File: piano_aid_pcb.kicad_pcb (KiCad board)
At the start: 2 copper layers, 101.6 x 63.5 mm, 0 parts

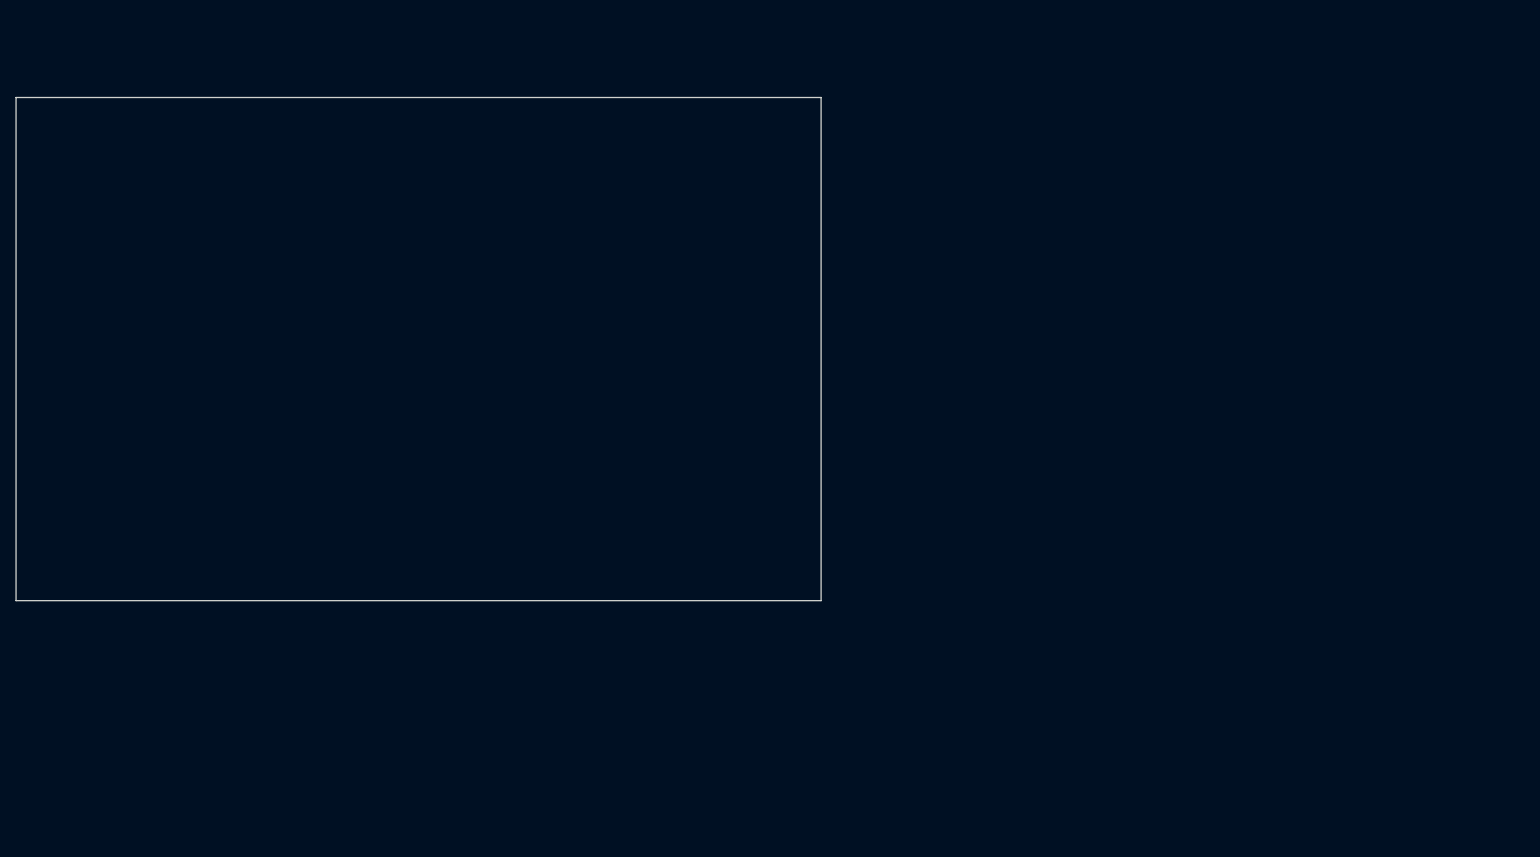
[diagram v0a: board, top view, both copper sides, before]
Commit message: Started board layout. Finished footprints
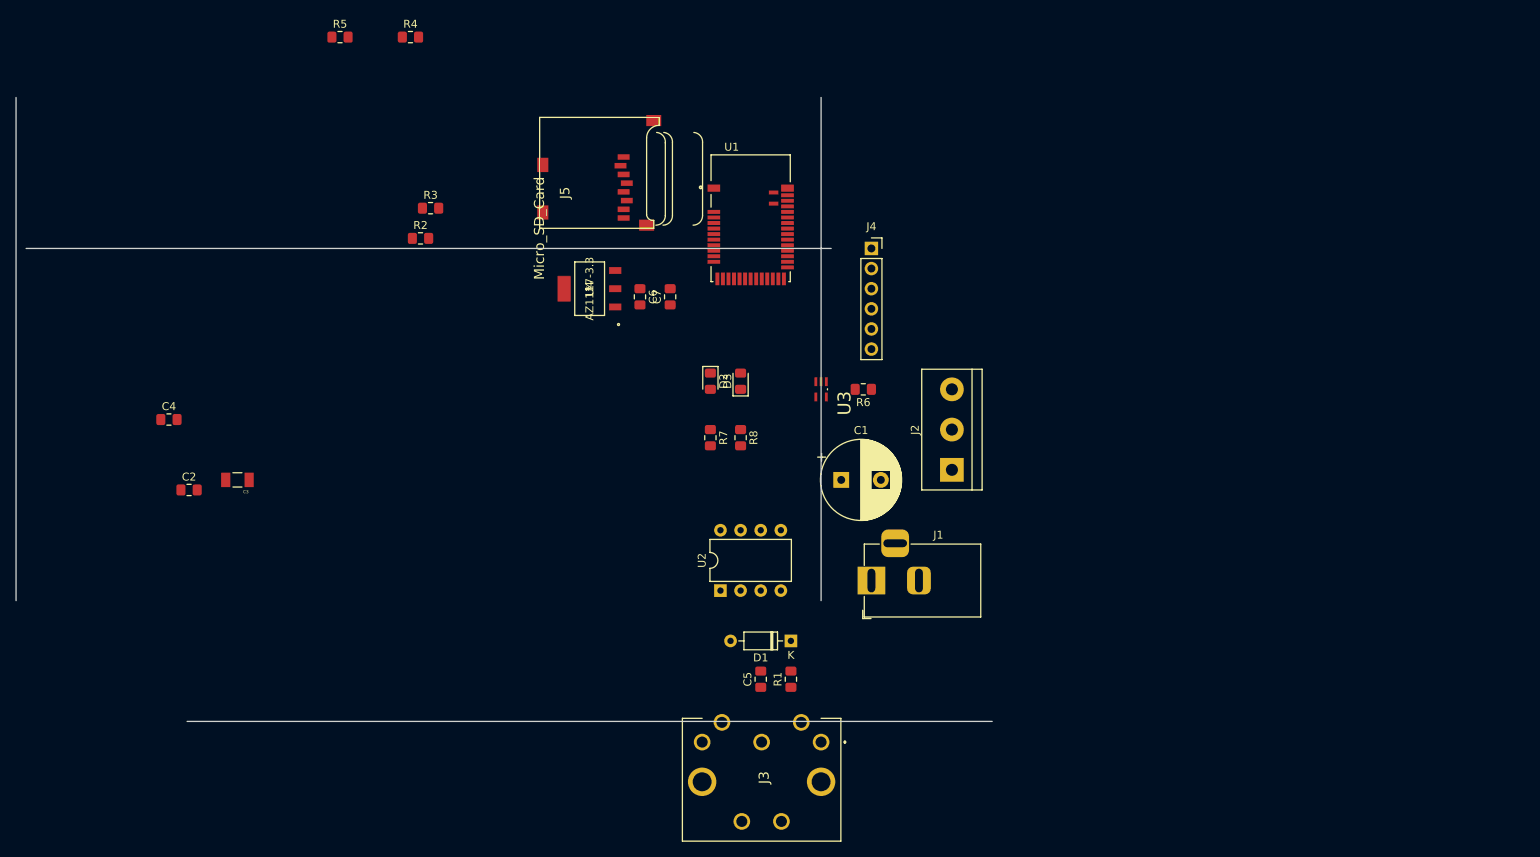
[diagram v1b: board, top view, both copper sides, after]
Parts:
- added C1: 1000µ, Capacitor_THT:CP_Radial_D10.0mm_P5.00mm, F.Cu at (205.7, 111.8)
- added C2: 0.1µ, Capacitor_SMD:C_0805_2012Metric_Pad1.15x1.40mm_HandSolder, F.Cu at (123.4, 113.0)
- added C3: 22µ, C1206C226M9PACTU:CAPC3216X110N, F.Cu at (129.5, 111.8)
- added C4: 10µ, Capacitor_SMD:C_0805_2012Metric_Pad1.15x1.40mm_HandSolder, F.Cu at (120.9, 104.1)
- added C5: 0.1µ, Capacitor_SMD:C_0805_2012Metric_Pad1.15x1.40mm_HandSolder, F.Cu at (195.6, 136.9)
- added C6: 10µ, Capacitor_SMD:C_0805_2012Metric_Pad1.15x1.40mm_HandSolder, F.Cu at (180.3, 88.7)
- added C7: 0.1µ, Capacitor_SMD:C_0805_2012Metric_Pad1.15x1.40mm_HandSolder, F.Cu at (184.2, 88.7)
- added D1: 1N914, Diode_THT:D_DO-35_SOD27_P7.62mm_Horizontal, F.Cu at (199.4, 132.1)
- added D2: LED_BLUE, LED_SMD:LED_0805_2012Metric_Pad1.15x1.40mm_HandSolder, F.Cu at (189.2, 99.3)
- added D3: LED_GREEN, LED_SMD:LED_0805_2012Metric_Pad1.15x1.40mm_HandSolder, F.Cu at (193.0, 99.3)
- added J1: Barrel_Jack_MountingPin, Connector_BarrelJack:BarrelJack_Horizontal, F.Cu at (209.6, 124.5)
- added J2: Screw_Terminal_01x03, TerminalBlock:TerminalBlock_bornier-3_P5.08mm, F.Cu at (219.7, 110.5)
- added J3: DIN-5_180degree, 57PC5F:57PC5F, F.Cu at (203.2, 144.8)
- added J4: Conn_01x06_Female, Connector_PinSocket_2.54mm:PinSocket_1x06_P2.54mm_Vertical, F.Cu at (209.6, 82.5)
- added J5: Micro_SD_Card, adafruit:MICROSD, F.Cu at (167.6, 80.0)
- added R1: 220, Resistor_SMD:R_0805_2012Metric_Pad1.15x1.40mm_HandSolder, F.Cu at (199.4, 136.9)
- added R2: 220, Resistor_SMD:R_0805_2012Metric_Pad1.15x1.40mm_HandSolder, F.Cu at (152.6, 81.3)
- added R3: 4.7k, Resistor_SMD:R_0805_2012Metric_Pad1.15x1.40mm_HandSolder, F.Cu at (153.9, 77.5)
- added R4: 10k, Resistor_SMD:R_0805_2012Metric_Pad1.15x1.40mm_HandSolder, F.Cu at (151.4, 55.9)
- added R5: 10k, Resistor_SMD:R_0805_2012Metric_Pad1.15x1.40mm_HandSolder, F.Cu at (142.5, 55.9)
- added R6: 440, Resistor_SMD:R_0805_2012Metric_Pad1.15x1.40mm_HandSolder, F.Cu at (208.5, 100.3)
- added R7: 220, Resistor_SMD:R_0805_2012Metric_Pad1.15x1.40mm_HandSolder, F.Cu at (189.2, 106.4)
- added R8: 220, Resistor_SMD:R_0805_2012Metric_Pad1.15x1.40mm_HandSolder, F.Cu at (193.0, 106.4)
- added U1: 317030213, micro:XCVR_317030213, F.Cu at (194.3, 78.7)
- added U2: 6N138, Package_DIP:DIP-8_W7.62mm, F.Cu at (190.5, 125.7)
- added U3: 74AHCT1G125SE-7, 74AHCT1G125SE-7:SOT65P210X110-5N, F.Cu at (203.2, 100.3)
- added U4: AZ1117-3.3, 2021-09-23_22-23-04:AZ1117IH-3.3TRG1, F.Cu at (174.0, 87.6)
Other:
- board size 101.6 x 63.5 mm -> 123.2 x 78.7 mm
- net class Default: clearance 0.2 -> 0.1524; trace_width 0.25 -> 0.1524; via_dia 0.8 -> 0.6858; via_drill 0.4 -> 0.3302
- rule pad_to_mask_clearance: 0 -> 0.0508
- rule trace_clearance: 0.2 -> 0.1524
- rule trace_min: 0.2 -> 0.1524
- rule via_min_drill: 0.3 -> 0.254
- rule via_min_size: 0.4 -> 0.508

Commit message: Made PCB. Not happy with the traces, may try again. For now this is 95% complete.
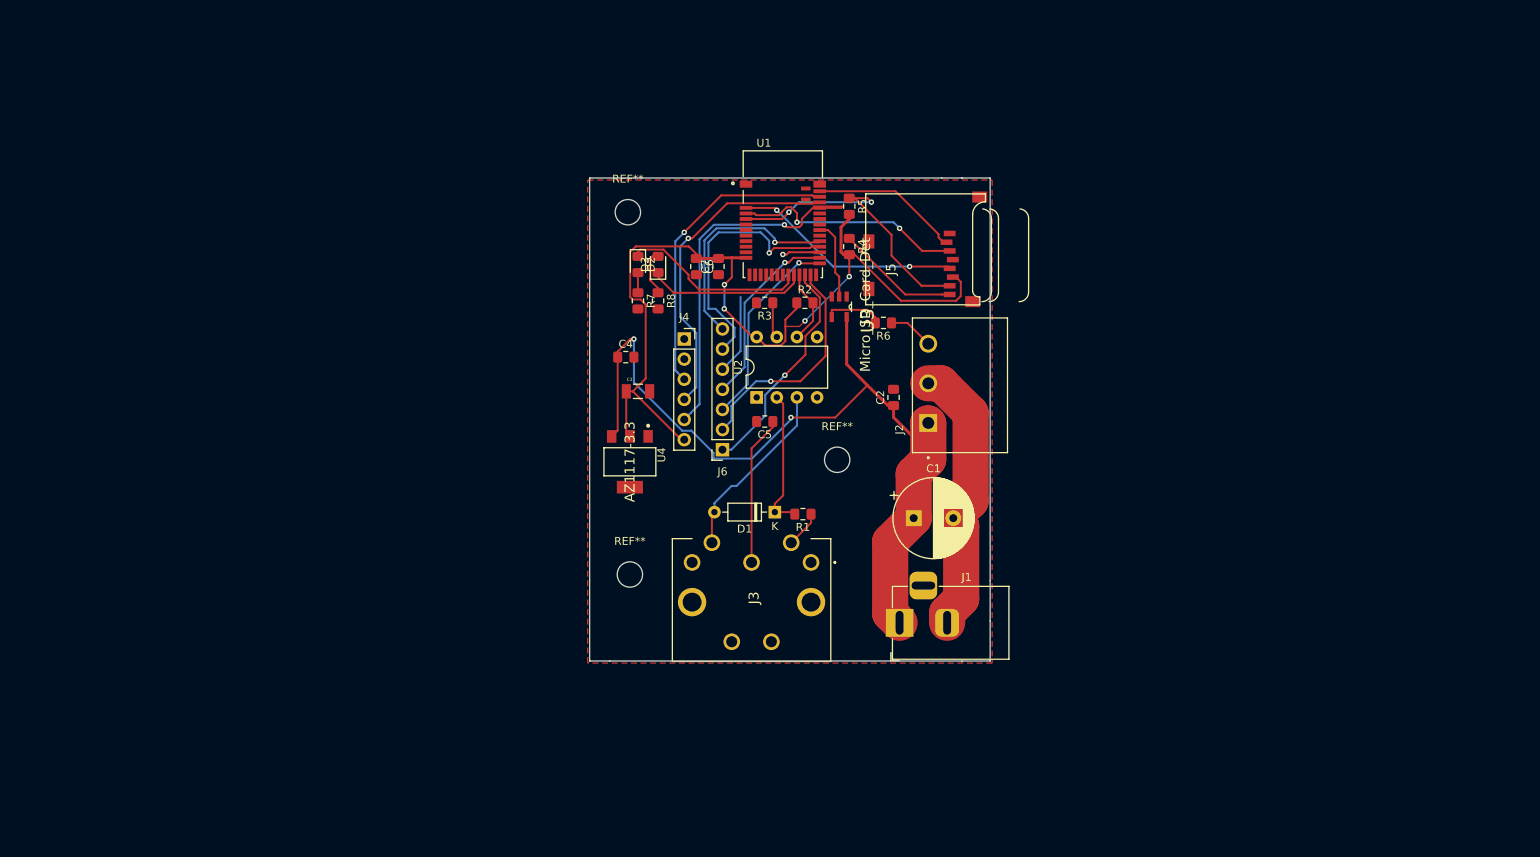
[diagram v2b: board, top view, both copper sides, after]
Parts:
- added J6: Conn_01x07_Female, Connector_PinSocket_2.54mm:PinSocket_1x07_P2.54mm_Vertical, F.Cu at (190.8, 108.0)
- added REF**: MountingHole_3.2mm_M3, MountingHole:MountingHole_3.2mm_M3, F.Cu at (179.1, 123.7)
- added REF**: MountingHole_3.2mm_M3, MountingHole:MountingHole_3.2mm_M3, F.Cu at (205.2, 109.2)
- added REF**: MountingHole_3.2mm_M3, MountingHole:MountingHole_3.2mm_M3, F.Cu at (178.8, 78.0)
- J2: value Screw_Terminal_01x03 -> 796644-3; footprint TerminalBlock:TerminalBlock_bornier-3_P5.08mm -> 796644-3:TE_796644-3
- J5: value Micro_SD_Card -> Micro_SD_Card_Det
- U3: value 74AHCT1G125SE-7 -> 74AHCT1G125W5-7; footprint 74AHCT1G125SE-7:SOT65P210X110-5N -> 74AHCT1G125W5-7:SOT95P280X140-5N
- U4: footprint 2021-09-23_22-23-04:AZ1117IH-3.3TRG1 -> eec:Diodes_Inc.-SOT223-03_2017-0-MFG
- moved C2 89.7 mm to (212.3, 101.4), turned to 90 degrees
- moved R5 67.7 mm to (206.8, 77.2), turned to 270 degrees
- moved R4 61.4 mm to (206.8, 82.3), turned to 270 degrees
- moved C4 58.2 mm to (178.6, 96.3)
- moved C3 51.8 mm to (180.1, 100.6), turned to 0 degrees
- moved R2 49.2 mm to (201.2, 89.4)
- moved R3 43.8 mm to (196.1, 89.4), turned to 180 degrees
- moved J5 42.3 mm to (208.8, 89.7)
- moved C5 32.5 mm to (196.1, 104.4), turned to 180 degrees
- moved J4 26.2 mm to (185.9, 94.0)
- moved U2 24.8 mm to (195.1, 101.3)
- moved J3 22.7 mm to (201.9, 122.2)
- moved U4 22.4 mm to (179.1, 109.5), turned to 270 degrees
- moved R1 20.9 mm to (200.9, 116.1), turned to 180 degrees
- moved R8 20.2 mm to (182.6, 89.2)
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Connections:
- U1 pad 22: Net-(U1-Pad22) -> P9
- U1 pad 23: Net-(U1-Pad23) -> P10
- U1 pad 25: Net-(U1-Pad25) -> P11
- U1 pad 26: Net-(U1-Pad26) -> P12
- U1 pad 27: Net-(U1-Pad27) -> P13
- U1 pad 28: Net-(U1-Pad28) -> P14
- U1 pad 29: Net-(U1-Pad29) -> P15
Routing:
- net 3.3V: track 0.00 -> 113.0 mm, vias 0 -> 4
- net 5V: track 0.00 -> 103.8 mm, vias 0 -> 2
- net RESET: track 0.00 -> 46.9 mm, vias 0 -> 1
- net SWDCLK: track 0.00 -> 40.7 mm, vias 0 -> 1
- net SWDIO: track 0.00 -> 38.6 mm, vias 0 -> 1
- net DAT0: track 0.00 -> 38.5 mm, vias 0 -> 2
- net GND: track 0.00 -> 35.4 mm
- net P14: track 0.00 -> 33.0 mm, vias 0 -> 1
- net CMD: track 0.00 -> 29.2 mm, vias 0 -> 2
- net P10: track 0.00 -> 29.0 mm, vias 0 -> 1
- net Net-(J5-Pad5): track 0.00 -> 28.9 mm, vias 0 -> 2
- net P15: track 0.00 -> 28.6 mm, vias 0 -> 1
- net P9: track 0.00 -> 28.6 mm, vias 0 -> 1
- net P11: track 0.00 -> 25.2 mm, vias 0 -> 1
- net P12: track 0.00 -> 23.9 mm, vias 0 -> 1
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- added copper zone on F.Cu, net GND
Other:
- board size 123.2 x 78.7 mm -> 50.5 x 61 mm

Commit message: Completely re-traced and layed out board. Presenting PCB V2
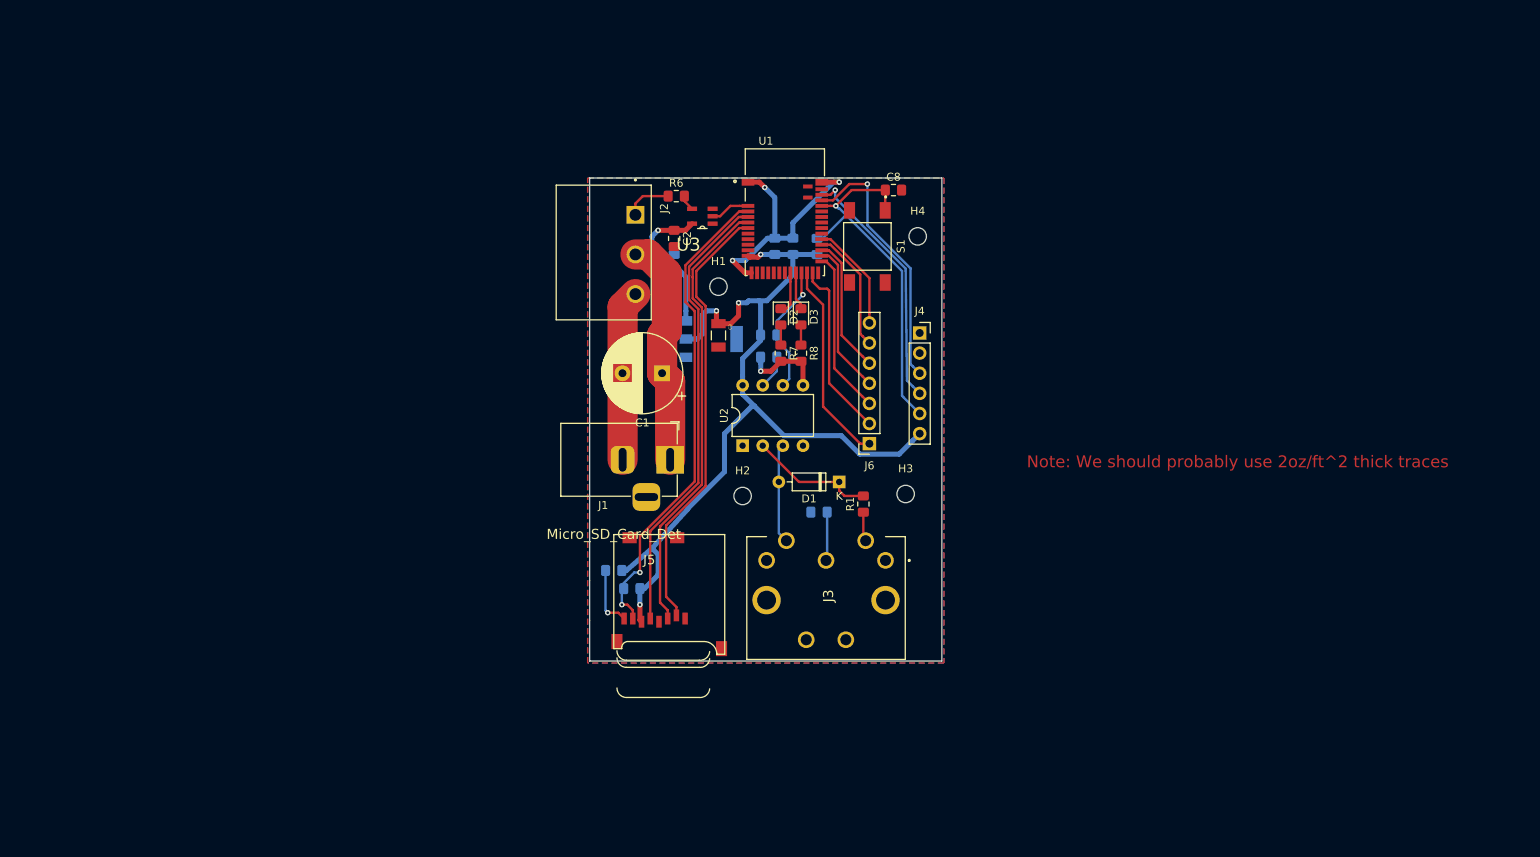
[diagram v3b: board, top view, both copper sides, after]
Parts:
- removed REF** (x3): MountingHole_3.2mm_M3, MountingHole:MountingHole_3.2mm_M3
- added C8: C, Capacitor_SMD:C_0805_2012Metric_Pad1.15x1.40mm_HandSolder, F.Cu at (212.3, 75.2)
- added H1: MountingHole, MountingHole:MountingHole_2.2mm_M2, F.Cu at (190.2, 87.4)
- added H2: MountingHole, MountingHole:MountingHole_2.2mm_M2, F.Cu at (193.3, 113.8)
- added H3: MountingHole, MountingHole:MountingHole_2.2mm_M2, F.Cu at (213.9, 113.5)
- added H4: MountingHole, MountingHole:MountingHole_2.2mm_M2, F.Cu at (215.4, 81.0)
- added R9: 10k, Resistor_SMD:R_0805_2012Metric_Pad1.15x1.40mm_HandSolder, B.Cu at (202.7, 82.3)
- added S1: GPTS203211B, 4-1437565-1:SW_4-1437565-1, F.Cu at (209.0, 82.3)
- C4, C5, C6, C7, R2, R3, R4, R5, U4: moved to B.Cu
- moved R5 55.5 mm to (179.3, 125.5), turned to 0 degrees
- moved R4 50.5 mm to (177.0, 123.2), turned to 0 degrees
- moved J2 48.0 mm to (175.8, 83.1), turned to 270 degrees
- moved J5 43.0 mm to (177.0, 118.6), turned to 0 degrees
- moved C1 36.6 mm to (183.1, 98.3), turned to 180 degrees
- moved J1 35.5 mm to (184.2, 109.2), turned to 0 degrees
- moved C2 34.2 mm to (184.7, 81.3), turned to 270 degrees
- moved R6 30.7 mm to (184.9, 75.9), turned to 0 degrees
- moved J4 29.7 mm to (215.6, 93.2)
- moved U3 20.7 mm to (188.2, 78.5), turned to 180 degrees
- moved D2 19.2 mm to (198.1, 91.2)
- moved D3 19.2 mm to (200.7, 91.2), turned to 270 degrees
- moved R7 19.2 mm to (198.1, 95.8)
- moved R8 19.2 mm to (200.7, 95.8)
- moved U4 18.6 mm to (189.3, 94.0), turned to 0 degrees
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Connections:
- net Net-(R2-Pad2) renamed MIDI_DIN
- J2 pad 1: 5V -> LED_CONTROL_OUT
- J2 pad 2: GND -> 5V
- J2 pad 3: LED_CONTROL_OUT -> GND
- J4 pad 3: SWDIO -> SWDCLK
- J4 pad 4: SWDCLK -> SWDIO
- J5 pad 2: Net-(J5-Pad2) -> CD
- J5 pad 5: Net-(J5-Pad5) -> CLK
- U1 pad 2: Net-(J5-Pad5) -> LED_CONTROL_IN
- U1 pad 3: CMD -> DAT0
- U1 pad 38: Net-(J5-Pad2) -> Net-(U1-Pad38)
- U1 pad 4: DAT0 -> CLK
- U1 pad 5: Net-(U1-Pad5) -> CMD
- U1 pad 6: Net-(U1-Pad6) -> CD
- U3 pad 2: Net-(U1-Pad31) -> LED_CONTROL_IN
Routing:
- net CLK: track 0.00 -> 58.4 mm
- net CD: track 0.00 -> 55.3 mm
- net 5V: track 103.8 -> 50.3 mm, vias 2 -> 1
- net GND: track 35.4 -> 65.4 mm, vias 0 -> 4
- net Net-(J5-Pad5): track 28.9 -> 0.00 mm, vias 2 -> 0
- net CMD: track 29.2 -> 57.5 mm, vias 2 -> 0
- net DAT0: track 38.5 -> 61.9 mm
- net Net-(J5-Pad2): track 18.9 -> 0.00 mm
- net Net-(D2-Pad1): track 23.5 -> 5.43 mm
- net P14: track 33.0 -> 15.5 mm, vias 1 -> 0
- net Net-(D3-Pad1): track 20.1 -> 4.79 mm
- net P15: track 28.6 -> 13.7 mm, vias 1 -> 0
- net Net-(C5-Pad1): track 18.9 -> 6.15 mm
- net Net-(D1-Pad2): track 23.1 -> 12.6 mm
- net Net-(U1-Pad31): track 10.0 -> 0.00 mm
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- added copper zone on B.Cu, net GND
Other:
- board size 50.5 x 61 mm -> 44.4 x 61 mm
- board text added: "Note: We should probably use 2oz/ft^2 thick traces"
